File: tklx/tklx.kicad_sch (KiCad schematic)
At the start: 190 parts

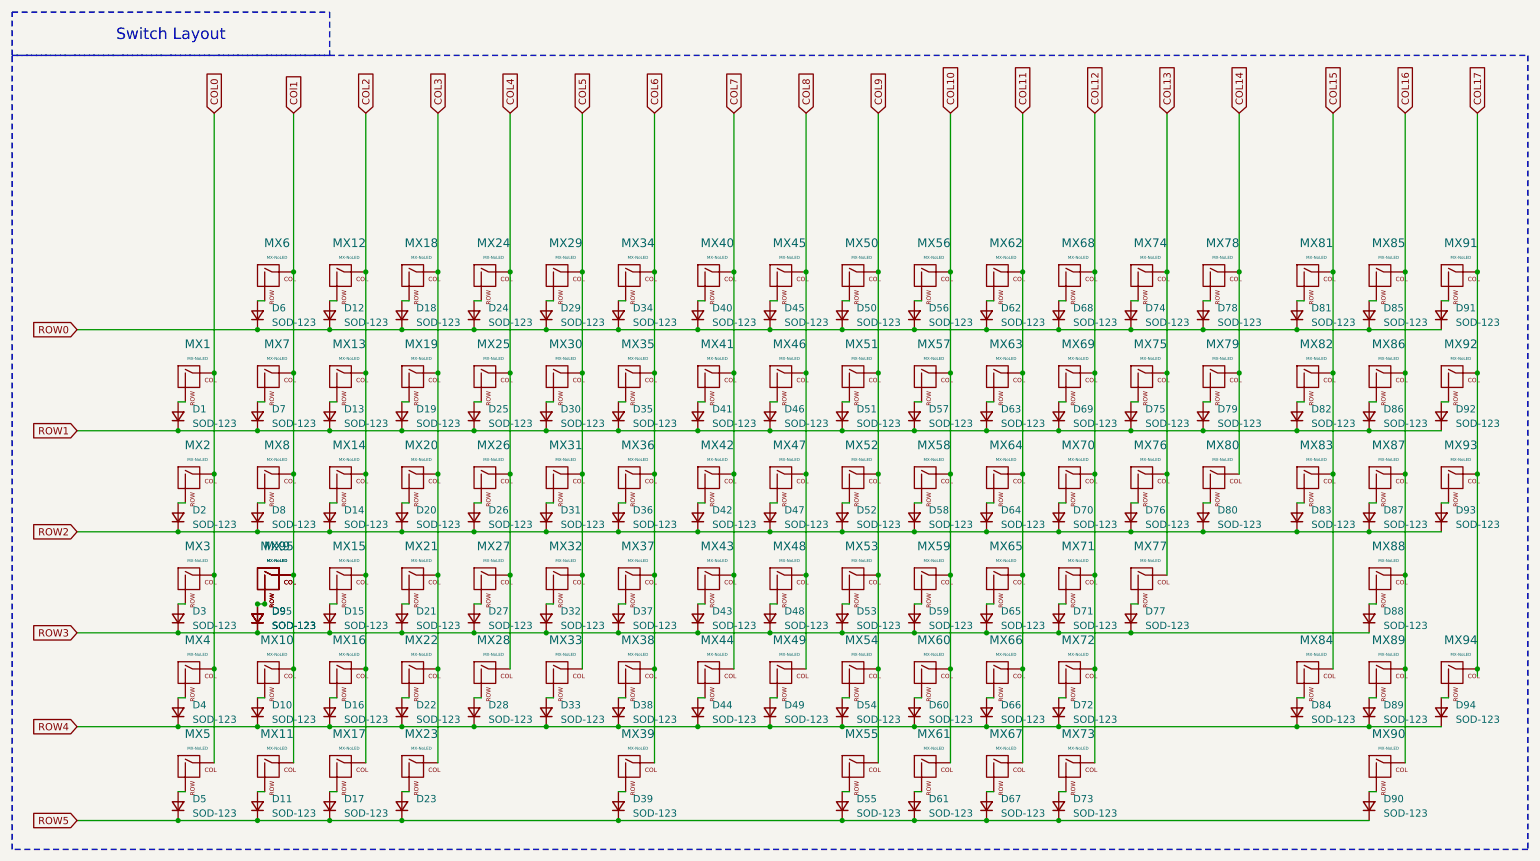
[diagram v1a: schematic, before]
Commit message: finished keyswitch layout
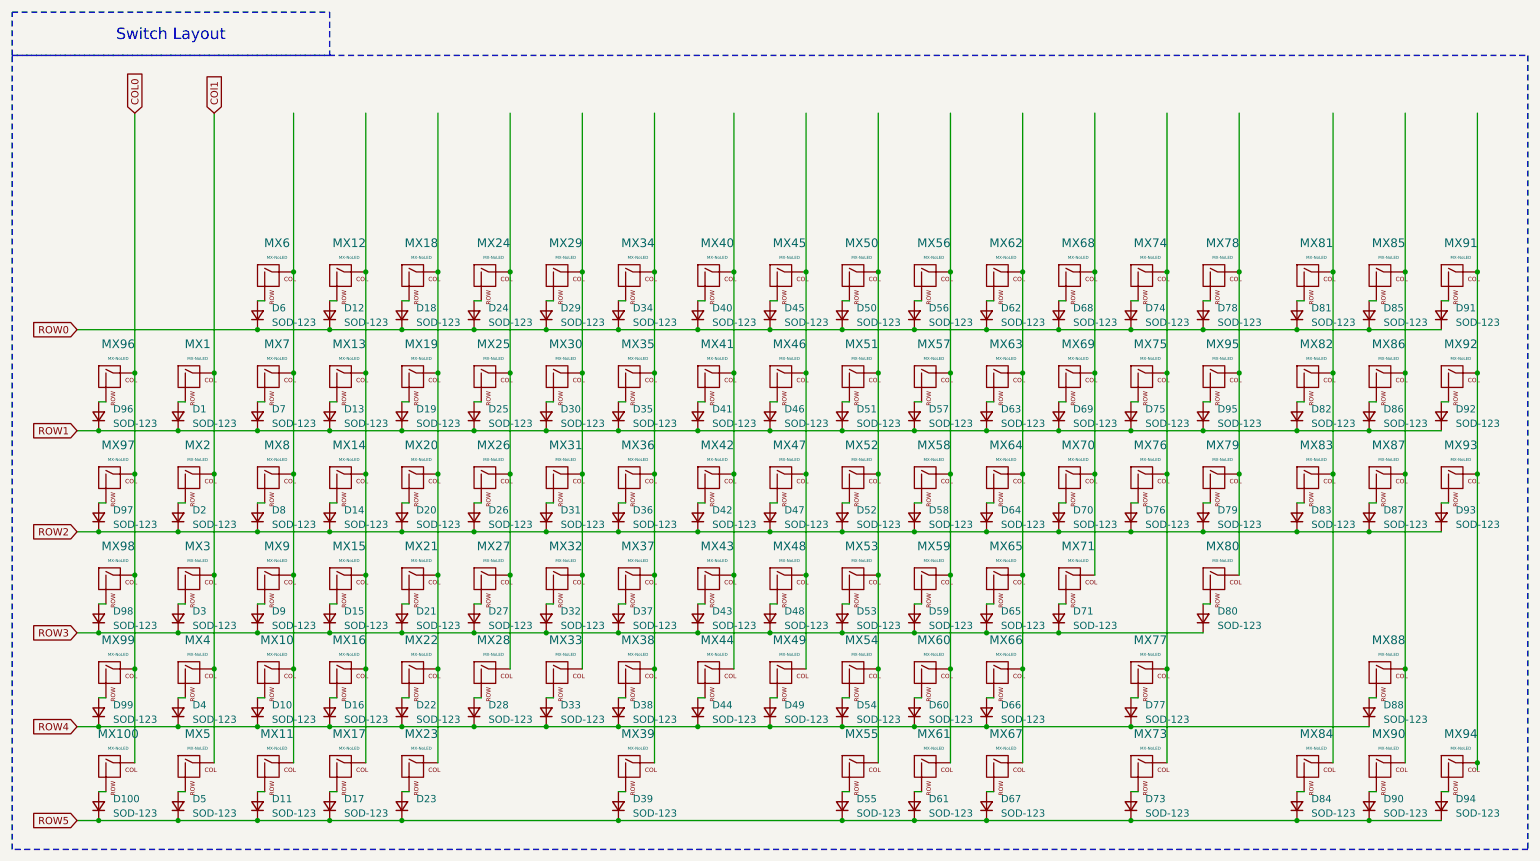
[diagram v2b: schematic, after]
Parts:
- removed D72, D89: SOD-123, Diode_SMD:D_SOD-123, symbol Device:D_Small
- removed MX72, MX89: MX-NoLED, MX_Only:MXOnly-1U-NoLED, symbol MX_Alps_Hybrid:MX-NoLED
- added D100, D96, D97, D98, D99: SOD-123, Diode_SMD:D_SOD-123, symbol Device:D_Small
- added MX100, MX96, MX97, MX98, MX99: MX-NoLED, MX_Only:MXOnly-1U-NoLED, symbol MX_Alps_Hybrid:MX-NoLED
- MX95: footprint MX_Only:MXOnly-1U-NoLED -> MX_Only:MXOnly-2U-NoLED
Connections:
- net COL0: now also MX100.1 (COL), MX96.1 (COL), MX97.1 (COL), MX98.1 (COL), MX99.1 (COL); no longer MX1.1 (COL), MX2.1 (COL), MX3.1 (COL), MX4.1 (COL), MX5.1 (COL)
- net COl1: now also MX1.1 (COL), MX2.1 (COL), MX3.1 (COL), MX4.1 (COL), MX5.1 (COL); no longer MX10.1 (COL), MX11.1 (COL), MX6.1 (COL), MX7.1 (COL), MX8.1 (COL), MX9.1 (COL), MX95.1 (COL)
- net ROW1: now also D95.1 (K), D96.1 (K); no longer D79.1 (K)
- net ROW2: now also D79.1 (K), D97.1 (K); no longer D80.1 (K)
- net ROW3: now also D80.1 (K), D98.1 (K); no longer D77.1 (K), D88.1 (K), D95.1 (K)
- net ROW4: now also D77.1 (K), D88.1 (K), D99.1 (K); no longer D84.1 (K), D94.1 (K)
- net ROW5: now also D84.1 (K), D94.1 (K), D100.1 (K)
- net at D9.2 (A), MX9.2 (ROW): no longer D95.2 (A), MX95.2 (ROW)
- net COL10: no longer names the net of MX56.1 (COL), MX57.1 (COL), MX58.1 (COL), MX59.1 (COL), MX60.1 (COL), MX61.1 (COL)
- net COL11: no longer names the net of MX62.1 (COL), MX63.1 (COL), MX64.1 (COL), MX65.1 (COL), MX66.1 (COL), MX67.1 (COL)
- net COL12: no longer names the net of MX68.1 (COL), MX69.1 (COL), MX70.1 (COL), MX71.1 (COL)
- net COL12: no longer MX73.1 (COL)
- net COL13: no longer names the net of MX74.1 (COL), MX75.1 (COL), MX76.1 (COL), MX77.1 (COL)
- net COL13: now also MX73.1 (COL)
- net COL14: no longer names the net of MX78.1 (COL), MX79.1 (COL), MX80.1 (COL)
- net COL14: now also MX95.1 (COL)
- net COL15: no longer names the net of MX81.1 (COL), MX82.1 (COL), MX83.1 (COL), MX84.1 (COL)
- net COL16: no longer names the net of MX85.1 (COL), MX86.1 (COL), MX87.1 (COL), MX88.1 (COL), MX90.1 (COL)
- net COL17: no longer names the net of MX91.1 (COL), MX92.1 (COL), MX93.1 (COL), MX94.1 (COL)
- net COL2: no longer names the net of MX12.1 (COL), MX13.1 (COL), MX14.1 (COL), MX15.1 (COL), MX16.1 (COL), MX17.1 (COL)
- net COL3: no longer names the net of MX18.1 (COL), MX19.1 (COL), MX20.1 (COL), MX21.1 (COL), MX22.1 (COL), MX23.1 (COL)
- net COL4: no longer names the net of MX24.1 (COL), MX25.1 (COL), MX26.1 (COL), MX27.1 (COL), MX28.1 (COL)
- net COL5: no longer names the net of MX29.1 (COL), MX30.1 (COL), MX31.1 (COL), MX32.1 (COL), MX33.1 (COL)
- net COL6: no longer names the net of MX34.1 (COL), MX35.1 (COL), MX36.1 (COL), MX37.1 (COL), MX38.1 (COL), MX39.1 (COL)
- net COL7: no longer names the net of MX40.1 (COL), MX41.1 (COL), MX42.1 (COL), MX43.1 (COL), MX44.1 (COL)
- net COL8: no longer names the net of MX45.1 (COL), MX46.1 (COL), MX47.1 (COL), MX48.1 (COL), MX49.1 (COL)
- net COL9: no longer names the net of MX50.1 (COL), MX51.1 (COL), MX52.1 (COL), MX53.1 (COL), MX54.1 (COL), MX55.1 (COL)
- new net: D97.2 (A), MX97.2 (ROW)
- new net: D96.2 (A), MX96.2 (ROW)
- new net: D99.2 (A), MX99.2 (ROW)
- new net: MX10.1 (COL), MX11.1 (COL), MX6.1 (COL), MX7.1 (COL), MX8.1 (COL), MX9.1 (COL)
- new net: D98.2 (A), MX98.2 (ROW)
- new net: D95.2 (A), MX95.2 (ROW)
- new net: D100.2 (A), MX100.2 (ROW)
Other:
- moved on the sheet: D73, D77, D79, D80, D84, D88, D94, MX73, MX77, MX79, MX80, MX84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

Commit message: finished microcontroller layout
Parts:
- removed D78: SOD-123, Diode_SMD:D_SOD-123, symbol Device:D_Small
- removed MX78: MX-NoLED, MX_Only:MXOnly-1U-NoLED, symbol MX_Alps_Hybrid:MX-NoLED
- added C1, C2: 1u, symbol Device:C_Small
- added C10, C11: 22p, symbol Device:C_Small
- added C12, C3, C4: 1uF, symbol Device:C_Small
- added C5: 10uF, symbol Device:C_Small
- added C6, C7, C8, C9: 0.1uF, symbol Device:C_Small
- added F1: Fuse_Small, symbol Device:Fuse_Small
- added J1: USB_C_Receptacle_USB2.0_14P, symbol Connector:USB_C_Receptacle_USB2.0_14P
- added J2: Conn_01x04, symbol Connector_Generic:Conn_01x04
- added J3: Conn_01x05, symbol Connector_Generic:Conn_01x05
- added R1, R2, R6, R8, R9: 5.1k, symbol Device:R_Small
- added R3, R4: 27, symbol Device:R_Small
- added R5, R7: 1K, symbol Device:R_Small
- added SW1, SW2: SW_Push, symbol Switch:SW_Push
- added U1: RP2040, Package_DFN_QFN:QFN-56-1EP_7x7mm_P0.4mm_EP3.2x3.2mm, symbol MCU_RaspberryPi:RP2040
- added U2: XC6206PxxxMR, Package_TO_SOT_SMD:SOT-23-3, symbol Regulator_Linear:XC6206PxxxMR
- added U3: SRV05-4, Package_TO_SOT_SMD:SOT-23-6, symbol Power_Protection:SRV05-4
- added U4: W25Q128JVS, Package_SO:SOIC-8_5.23x5.23mm_P1.27mm, symbol Memory_Flash:W25Q128JVS
- added Y1: Crystal_GND24, symbol Device:Crystal_GND24
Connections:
- net COL0: now also U1.2 (GPIO0)
- net COl1: now also U1.3 (GPIO1)
- net ROW0: now also U1.30 (GPIO19)
- net ROW1: now also U1.31 (GPIO20)
- net ROW2: now also U1.32 (GPIO21)
- net ROW3: now also U1.34 (GPIO22)
- net ROW4: now also U1.35 (GPIO23)
- net ROW5: now also U1.36 (GPIO24)
- net COL6: now reaches MX29.1 (COL), MX30.1 (COL), MX31.1 (COL), MX32.1 (COL), MX33.1 (COL)
- net COL6: now also U1.8 (GPIO6)
- net COL9: now reaches MX45.1 (COL), MX46.1 (COL), MX47.1 (COL), MX48.1 (COL), MX49.1 (COL)
- net COL9: now also U1.12 (GPIO9)
- net COL11: now reaches MX56.1 (COL), MX57.1 (COL), MX58.1 (COL), MX59.1 (COL), MX60.1 (COL), MX61.1 (COL)
- net COL11: now also U1.14 (GPIO11)
- net COL4: now reaches MX18.1 (COL), MX19.1 (COL), MX20.1 (COL), MX21.1 (COL), MX22.1 (COL), MX23.1 (COL)
- net COL4: now also U1.6 (GPIO4)
- net COL18: now reaches MX91.1 (COL), MX92.1 (COL), MX93.1 (COL), MX94.1 (COL)
- net COL18: now also U1.29 (GPIO18)
- net COL3: now reaches MX12.1 (COL), MX13.1 (COL), MX14.1 (COL), MX15.1 (COL), MX16.1 (COL), MX17.1 (COL)
- net COL3: now also U1.5 (GPIO3)
- net COL16: now reaches MX81.1 (COL), MX82.1 (COL), MX83.1 (COL), MX84.1 (COL)
- net COL16: now also U1.27 (GPIO16)
- net COL8: now reaches MX40.1 (COL), MX41.1 (COL), MX42.1 (COL), MX43.1 (COL), MX44.1 (COL)
- net COL8: now also U1.11 (GPIO8)
- net COL12: now reaches MX62.1 (COL), MX63.1 (COL), MX64.1 (COL), MX65.1 (COL), MX66.1 (COL), MX67.1 (COL)
- net COL12: now also U1.15 (GPIO12)
- net COL15: now reaches MX79.1 (COL), MX80.1 (COL), MX95.1 (COL)
- net COL15: now also U1.18 (GPIO15)
- net COL14: now reaches MX73.1 (COL), MX74.1 (COL), MX75.1 (COL), MX76.1 (COL), MX77.1 (COL)
- net COL14: now also U1.17 (GPIO14)
- net COL2: now reaches MX10.1 (COL), MX11.1 (COL), MX6.1 (COL), MX7.1 (COL), MX8.1 (COL), MX9.1 (COL)
- net COL2: now also U1.4 (GPIO2)
- net COL10: now reaches MX50.1 (COL), MX51.1 (COL), MX52.1 (COL), MX53.1 (COL), MX54.1 (COL), MX55.1 (COL)
- net COL10: now also U1.13 (GPIO10)
- net COL17: now reaches MX85.1 (COL), MX86.1 (COL), MX87.1 (COL), MX88.1 (COL), MX90.1 (COL)
- net COL17: now also U1.28 (GPIO17)
- net COL5: now reaches MX24.1 (COL), MX25.1 (COL), MX26.1 (COL), MX27.1 (COL), MX28.1 (COL)
- net COL5: now also U1.7 (GPIO5)
- net COL7: now reaches MX34.1 (COL), MX35.1 (COL), MX36.1 (COL), MX37.1 (COL), MX38.1 (COL), MX39.1 (COL)
- net COL7: now also U1.9 (GPIO7)
- net COL13: now reaches MX68.1 (COL), MX69.1 (COL), MX70.1 (COL), MX71.1 (COL)
- net COL13: now also U1.16 (GPIO13)
- new net: C11.2, R5.1, Y1.1
- new net: J1.B5 (CC2), R1.1
- new net: R7.2, SW2.2
- new net: J1.A5 (CC1), R2.1
- new net: R4.2, U1.46 (USB_DM)
- new net: R8.1, R9.2
- new net: R3.2, U1.47 (USB_DP)
- new net +1V1: C3.1, C7.1, U1.23 (DVDD), U1.45 (VREG_VOUT), U1.50 (DVDD)
- new net +3.3V: R9.1, U1.1 (IOVDD), U1.10 (IOVDD), U1.22 (IOVDD), U1.33 (IOVDD), U1.42 (IOVDD), U1.43 (ADC_AVDD), U1.44 (VREG_IN), U1.48 (USB_VDD), U1.49 (IOVDD)
- new net +3V3: C12.1, C2.1, C4.1, C5.1, C6.1, C8.1, C9.1, J3.2 (Pin_2), R6.1, U2.2 (VO), U4.8 (VCC)
- new net +5V: C1.1, F1.2, J2.1 (Pin_1), U2.3 (VI), U3.5 (VP)
- new net D+: J1.A6 (D+), J1.B6 (D+), J2.3 (Pin_3), R3.1, U3.1 (IO1)
- new net D-: J1.A7 (D-), J1.B7 (D-), J2.2 (Pin_2), R4.1, U3.3 (IO2)
- new net GND: C1.2, C10.1, C11.1, C12.2, C2.2, C3.2, C4.2, C5.2, C6.2, C7.2, C8.2, C9.2, J1.A1 (GND), J1.A12 (GND), J1.B1 (GND), J1.B12 (GND), J1.S1 (SHIELD), J2.4 (Pin_4), J3.3 (Pin_3), R1.2, R2.2, SW1.1, SW2.1, U1.19 (TESTEN), U1.57 (GND), U2.1 (GND), U3.2 (VN), U4.4 (GND), Y1.2, Y1.4
- new net Q_100: U1.53 (QSPI_SD0), U4.5 (DI(IO0))
- new net Q_101: U1.55 (QSPI_SD1), U4.2 (DO(IO1))
- new net Q_102: U1.54 (QSPI_SD2), U4.3 (IO2)
- new net Q_103: U1.51 (QSPI_SD3), U4.7 (IO3)
- new net Q_CLK: U1.52 (QSPI_SCLK), U4.6 (CLK)
- new net Q_SEL: R7.1, R8.2, U1.56 (QSPI_SS), U4.1 (~{CS})
- new net RESET: J3.1 (Pin_1), R6.2, SW1.2, U1.26 (RUN)
- new net SWC: J3.4 (Pin_4), U1.24 (SWCLK)
- new net SWD: J3.5 (Pin_5), U1.25 (SWD)
- new net VBUS: F1.1, J1.A4 (VBUS), J1.A9 (VBUS), J1.B4 (VBUS), J1.B9 (VBUS)
- new net XIN: C10.2, U1.20 (XIN), Y1.3
- new net XOUT: R5.2, U1.21 (XOUT)
- no-connect marks 0 -> 7
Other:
- moved on the sheet: D1, D10, D100, D11, D12, D13, D14, D15, D16, D17, D18, D19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

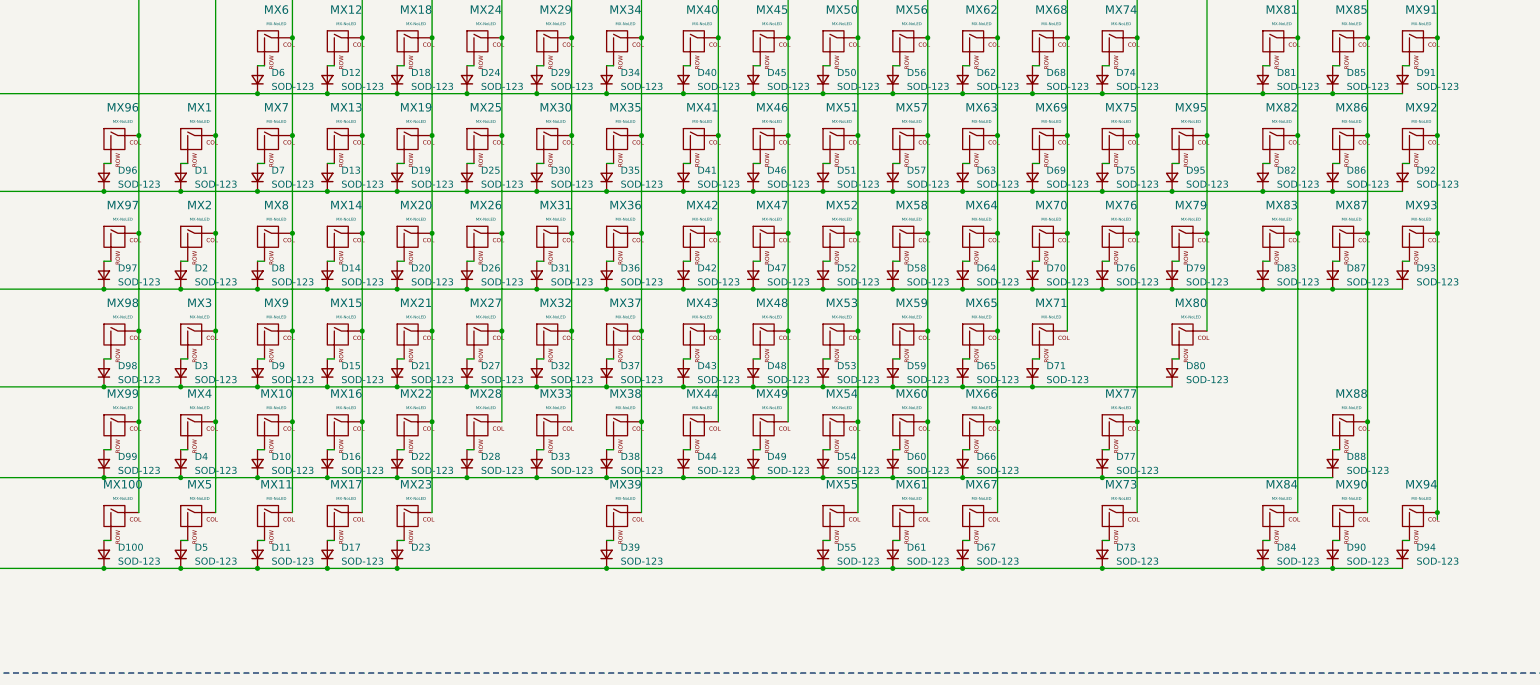
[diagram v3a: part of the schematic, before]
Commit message: added support for 7u and stepped caps
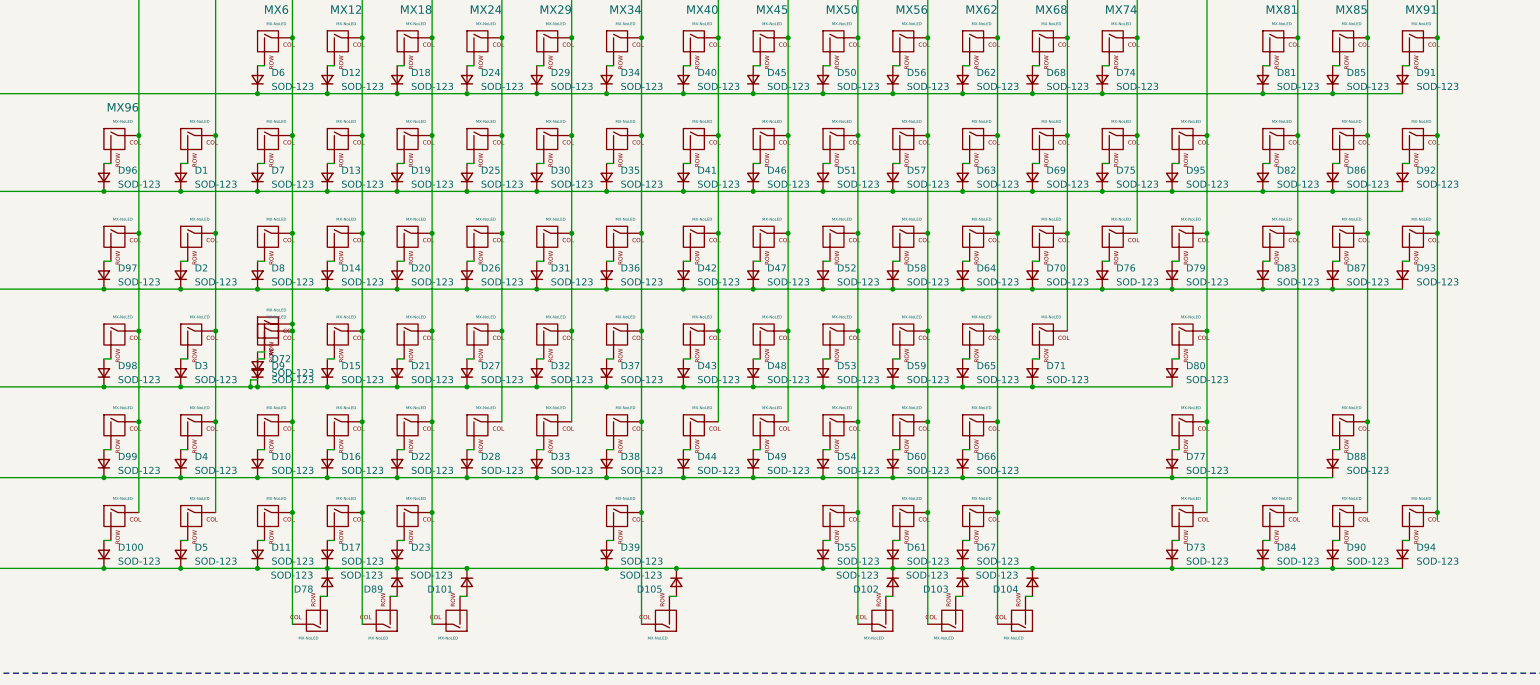
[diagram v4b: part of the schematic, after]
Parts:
- added D101, D102, D103, D104, D105, D72, D78, D89: SOD-123, Diode_SMD:D_SOD-123, symbol Device:D_Small
- added MX101, MX102, MX104, MX78: MX-NoLED, MX_Only:MXOnly-1.5U-NoLED, symbol MX_Alps_Hybrid:MX-NoLED
- added MX103, MX89: MX-NoLED, MX_Only:MXOnly-1U-NoLED, symbol MX_Alps_Hybrid:MX-NoLED
- added MX105: MX-NoLED, MX_Only:MXOnly-7U-NoLED, symbol MX_Alps_Hybrid:MX-NoLED
- added MX72: MX-NoLED, MX_Only:MXOnly-1.75U-NoLED, symbol MX_Alps_Hybrid:MX-NoLED
- C1, C10, C11, C12, C2, C3, C4, C6, C7, C8, C9: footprint (none) -> Capacitor_SMD:C_0402_1005Metric
- C5: footprint (none) -> Capacitor_SMD:C_0603_1608Metric
- F1: footprint (none) -> Fuse:Fuse_1206_3216Metric
- J1: footprint (none) -> Connector_USB:USB_C_Receptacle_HRO_TYPE-C-31-M-12
- J2: footprint (none) -> Connector_JST:JST_SH_SM04B-SRSS-TB_1x04-1MP_P1.00mm_Horizontal
- J3: footprint (none) -> Connector_PinHeader_2.54mm:PinHeader_1x05_P2.54mm_Vertical
- MX9: footprint MX_Only:MXOnly-1.75U-NoLED -> MX_Only:MXOnly-1.75U
- R1, R2, R3, R4, R5, R6, R7, R8, R9: footprint (none) -> Resistor_SMD:R_0402_1005Metric
- SW1, SW2: footprint (none) -> Button_Switch_SMD:SW_Push_SPST_NO_Alps_SKRK
- Y1: footprint (none) -> Crystal:Crystal_SMD_3225-4Pin_3.2x2.5mm
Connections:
- net COL10: now also MX102.1 (COL)
- net COL11: now also MX103.1 (COL)
- net COL12: now also MX104.1 (COL)
- net COL14: no longer MX73.1 (COL), MX77.1 (COL)
- net COL15: now also MX73.1 (COL), MX77.1 (COL)
- net COL2: now also MX72.1 (COL), MX78.1 (COL)
- net COL3: now also MX89.1 (COL)
- net COL4: now also MX101.1 (COL)
- net COL7: now also MX105.1 (COL)
- net ROW3: now also D72.1 (K)
- net ROW5: now also D101.1 (K), D102.1 (K), D103.1 (K), D104.1 (K), D105.1 (K), D78.1 (K), D89.1 (K)
- new net: D103.2 (A), MX103.2 (ROW)
- new net: D78.2 (A), MX78.2 (ROW)
- new net: D101.2 (A), MX101.2 (ROW)
- new net: D102.2 (A), MX102.2 (ROW)
- new net: D104.2 (A), MX104.2 (ROW)
- new net: D89.2 (A), MX89.2 (ROW)
- new net: D105.2 (A), MX105.2 (ROW)
- new net: D72.2 (A), MX72.2 (ROW)
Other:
- moved on the sheet: D73, D77

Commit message: flipped keys for tsangan layout to be on correct plane
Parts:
- MX9: footprint MX_Only:MXOnly-1.75U -> MX_Only:MXOnly-1.75U-NoLED
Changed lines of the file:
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@@
 			)
 		)
-		(property "Footprint" "MX_Only:MXOnly-1.75U"
+		(property "Footprint" "MX_Only:MXOnly-1.75U-NoLED"
 			(at 69.215 252.095 0)
 			(effects

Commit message: rotated keys for tsangan layout and stepped caps to be proper orientation.
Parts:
- removed C10, C11: 22p, Capacitor_SMD:C_0402_1005Metric, symbol Device:C_Small
- removed C12, C3, C4: 1uF, Capacitor_SMD:C_0402_1005Metric, symbol Device:C_Small
- removed C5: 10uF, Capacitor_SMD:C_0603_1608Metric, symbol Device:C_Small
- removed C6, C7, C8, C9: 0.1uF, Capacitor_SMD:C_0402_1005Metric, symbol Device:C_Small
- removed J3: Conn_01x05, Connector_PinHeader_2.54mm:PinHeader_1x05_P2.54mm_Vertical, symbol Connector_Generic:Conn_01x05
- removed R3, R4: 27, Resistor_SMD:R_0402_1005Metric, symbol Device:R_Small
- removed R5: 1K, Resistor_SMD:R_0402_1005Metric, symbol Device:R_Small
- removed U1: RP2040, Package_DFN_QFN:QFN-56-1EP_7x7mm_P0.4mm_EP3.2x3.2mm, symbol MCU_RaspberryPi:RP2040
- removed U4: W25Q128JVS, Package_SO:SOIC-8_5.23x5.23mm_P1.27mm, symbol Memory_Flash:W25Q128JVS
- removed Y1: Crystal_GND24, Crystal:Crystal_SMD_3225-4Pin_3.2x2.5mm, symbol Device:Crystal_GND24
- added U1: ESP32-S2, Package_DFN_QFN:QFN-56-1EP_7x7mm_P0.4mm_EP5.6x5.6mm, symbol PCM_Espressif:ESP32-S2
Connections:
- net COL10: now also MX45.1 (COL); no longer MX102.1 (COL), MX50.1 (COL)
- net COL11: now also MX102.1 (COL), MX50.1 (COL); no longer MX103.1 (COL), MX56.1 (COL)
- net COL12: now also MX56.1 (COL); no longer MX104.1 (COL), MX62.1 (COL), MX67.1 (COL)
- net COL13: now also MX103.1 (COL), MX62.1 (COL), MX67.1 (COL); no longer MX68.1 (COL)
- net COL14: now also MX68.1 (COL); no longer MX74.1 (COL)
- net COL15: now also MX104.1 (COL), MX74.1 (COL)
- net COL7: no longer MX34.1 (COL)
- net COL8: now also MX34.1 (COL); no longer MX40.1 (COL)
- net COL9: now also MX40.1 (COL); no longer MX45.1 (COL)
- net D+: now also U1.26 (GPIO20/ADC2_CH9/USB_D+)
- net D-: now also U1.25 (GPIO19/ADC2_CH8/USB_D-)
- net GND: now also U1.57 (GND)
- new net: U1.1 (VDDA), U1.51 (VDDA), U1.54 (VDDA)
- new net: U1.3 (VDD3P3), U1.4 (VDD3P3)
- no-connect marks 7 -> 2
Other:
- moved on the sheet: D101, D102, D103, D104, D34, D40, D45, D50, D56, D62, D67, D68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
